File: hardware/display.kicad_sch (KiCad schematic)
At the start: 1 part, among them J3 Display Connector

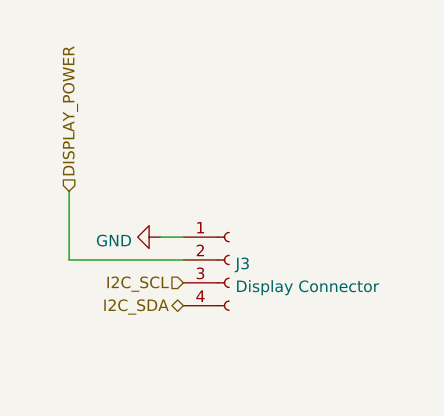
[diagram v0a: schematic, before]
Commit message: Updated schematic according to reference design
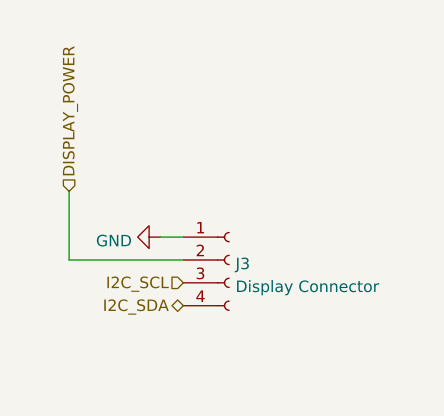
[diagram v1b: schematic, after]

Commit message: Added correct symbol and libraries for ADC
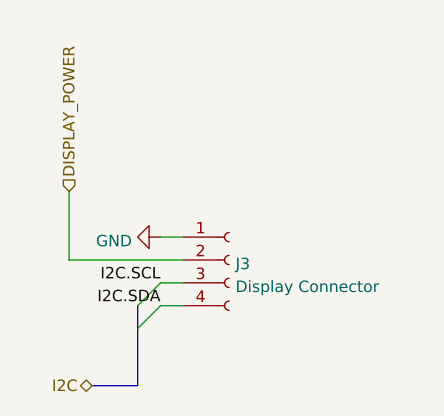
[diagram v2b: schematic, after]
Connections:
- net I2C_SCL renamed I2C.SCL
- net I2C_SDA renamed I2C.SDA
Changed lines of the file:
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@@
 	(generator_version "9.0")
 	(paper "A4")
+	(bus_entry
+		(at 109.22 81.28)
+		(size 2.54 -2.54)
+		(stroke
+			(width 0)
+			(type default)
+		)
+	)
+	(bus_entry
+		(at 109.22 78.74)
+		(size 2.54 -2.54)
+		(stroke
+			(width 0)
+			(type default)
+		)
+	)
 	(wire
 		(pts
@@
 		)
 	)
+	(bus
+		(pts
+			(xy 104.14 87.63) (xy 109.22 87.63)
+		)
+		(stroke
+			(width 0)
+			(type default)
+		)
+	)
 	(wire
 		(pts
@@
 	(wire
 		(pts
+			(xy 114.3 78.74) (xy 111.76 78.74)
+		)
+		(stroke
+			(width 0)
+			(type default)
+		)
+	)
+	(bus
+		(pts
+			(xy 109.22 81.28) (xy 109.22 87.63)
+		)
+		(stroke
+			(width 0)
+			(type default)
+		)
+	)
+	(wire
+		(pts
+			(xy 114.3 76.2) (xy 111.76 76.2)
+		)
+		(stroke
+			(width 0)
+			(type default)
+		)
+	)
+	(bus
+		(pts
+			(xy 109.22 78.74) (xy 109.22 81.28)
+		)
+		(stroke
+			(width 0)
+			(type default)
+		)
+	)
+	(wire
+		(pts
 			(xy 101.6 73.66) (xy 101.6 66.04)
 		)
@@
 		)
 	)
-	(hierarchical_label "I2C_SCL"
-		(shape input)
-		(at 114.3 76.2 180)
-		(effects
-			(font
-				(size 1.27 1.27)
-			)
-			(justify right)
-		)
-	)
-	(hierarchical_label "I2C_SDA"
+	(label "I2C.SDA"
+		(at 111.76 78.74 180)
+		(effects
+			(font
+				(size 1.27 1.27)
+			)
+			(justify right bottom)
+		)
+	)
+	(label "I2C.SCL"
+		(at 111.76 76.2 180)
+		(effects
+			(font
+				(size 1.27 1.27)
+			)
+			(justify right bottom)
+		)
+	)
+	(hierarchical_label "I2C"
 		(shape bidirectional)
-		(at 114.3 78.74 180)
+		(at 104.14 87.63 180)
 		(effects
 			(font
@@
 					(size 1.27 1.27)
 				)
+				(hide yes)
 			)
 		)
@@
 			)
 		)
-		(property "Description" ""
+		(property "Description" "Power symbol creates a global label with name \"GND\" , ground"
 			(at 111.76 71.12 0)
 			(effects
@@
 					(size 1.27 1.27)
 				)
-			)
-		)
+				(hide yes)
+			)
+		)

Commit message: Regenerated reference designators, changed to rail-to-rail op-amps
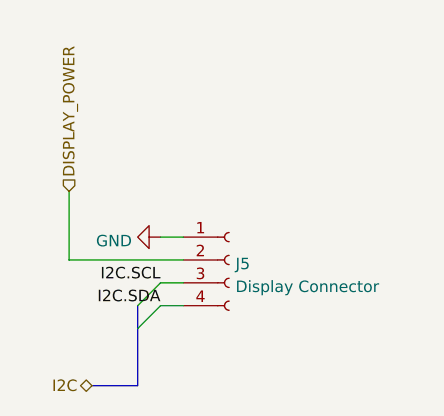
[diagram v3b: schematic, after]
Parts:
- renumbered J3 to J5
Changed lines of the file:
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@@
 		(dnp no)
 		(fields_autoplaced yes)
-		(property "Reference" "J3"
+		(property "Reference" "J5"
 			(at 120.0912 74.0953 0)
 			(effects
@@
 			(project ""
 				(path "/adf38c8f-bada-4838-acc6-e6af19946742/54892cf2-0f54-4d61-9dbf-907e3012c3d6"
-					(reference "J3")
+					(reference "J5")
 					(unit 1)
 				)
@@
 		(dnp no)
 		(fields_autoplaced yes)
-		(property "Reference" "#PWR0112"
+		(property "Reference" "#PWR012"
 			(at 105.41 71.12 0)
 			(effects
@@
 			(project ""
 				(path "/adf38c8f-bada-4838-acc6-e6af19946742/54892cf2-0f54-4d61-9dbf-907e3012c3d6"
-					(reference "#PWR0112")
+					(reference "#PWR012")
 					(unit 1)
 				)

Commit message: Major changes to schematic
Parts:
- J5: footprint Custom:0.96'' Display -> Connector_PinHeader_2.54mm:PinHeader_1x04_P2.54mm_Vertical
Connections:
- net I2C.SCL renamed SCL
- net I2C.SDA renamed SDA
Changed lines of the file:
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@@
 		)
 	)
-	(label "I2C.SDA"
+	(label "SDA"
 		(at 111.76 78.74 180)
 		(effects
@@
 		)
 	)
-	(label "I2C.SCL"
+	(label "SCL"
 		(at 111.76 76.2 180)
 		(effects
@@
 		)
 	)
-	(hierarchical_label "I2C"
+	(hierarchical_label "{I2C}"
 		(shape bidirectional)
 		(at 104.14 87.63 180)
@@
 			)
 		)
-		(property "Footprint" "Custom:0.96'' Display"
+		(property "Footprint" "Connector_PinHeader_2.54mm:PinHeader_1x04_P2.54mm_Vertical"
 			(at 119.38 73.66 0)
 			(effects
